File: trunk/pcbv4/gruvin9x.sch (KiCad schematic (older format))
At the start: 220 parts, among them IC1 ATMEGA2560-A_GRUVIN, J4 JUMPER_2W, K1 CONN_3, K2 CONN_3, K3 CONN_3, K4 CONN_3, P1 CONN_3X2, P10 CONN_5X2, P11 CONN_1, P12 CONN_4, P13 CONN_8, P14 CONN_2, P15 CONN_4, P16 CONN_1, P17 CONN_1, P18 CONN_2, P19 CONN_8, P2 CONN_5, P20 CONN_8, P21 CONN_4, P22 CONN_1, P23 CONN_1, P24 CONN_1, P25 CONN_1, P26 CONN_1, P27 CONN_2, P3 CONN_6, P4 CONN_9, P5 CONN_9, P6 CONN_6, P7 CONN_12, P8 CONN_30_LCD_GRUVIN, P9 CONN_1, Q1 BC847C, Q2 BC847C, Q3 BC857C, Q4 BC847C, Q5 BC847C, Q6 BC847C, Q7 BC847C, SW1 SW_PUSH, SW2 SW_PUSH, SW3 SW_PUSH, SW4 SW_PUSH, SW5 SW_PUSH, SW6 SW_PUSH, U1 78L05, U3 LN-6206-30, U4 TPS77601, X1 16MHz

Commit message: The keyboard 4x4 matrix has been removed to make the V4 board truly plug in compatible with the Tx. This has cost us 6 of our spare pins but well worth it in terms of palatability for a would be producer of the board. BOM updated. LED backlight finalized. Minor corrections of the footprint for the UK coin cell socket. More minor changes to...
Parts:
- removed D10, D11, D12, D13, D14, D15, D3, D4, D5, D6, D7, D8, D9: DIODESCH, symbol DIODESCH
- removed P19: CONN_8, symbol CONN_8
- removed P27: CONN_2, CONN_2MM_2x1, symbol CONN_2
- removed Q6: BC847C, SOT23-BCE, symbol BC847C
- added C37, C38, C39, C40, C41, C42, C43, C53, C54, C55, C56, C57, C58, C59, C60, C61: 0.1uF, symbol C
- added J1: JUMPER_2W, symbol JUMPER_2W
- added K5: CONN_3, symbol CONN_3
- added Q6: Si2319DS, symbol MOSFET_P
- added R100, R86, R87, R88, R89, R90, R97, R98, R99: 200R, symbol R
- added R101: 5K1, symbol R
- added U2: 78L05, SOT89, symbol 78L05
- R78: value 0R -> 200R
- R85: value 5K1 -> 100K
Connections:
- net labels added: Spare5, Spare6
- net labels removed: J1, J2, KEY_X0, KEY_X1, KEY_X2, KEY_X3, KEY_Y0, KEY_Y1, KEY_Y2, KEY_Y3
- wire segments 651 -> 685
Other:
- note removed: "(previously GNDs)"
- note removed: "4x4 Switch Matrix"
- note removed: "NOTE: Pull-ups for \nY0-Y3 MUST be off"
- note removed: "Navigation Buttons (reconfigured)"
- note removed: "Trim Switches"
- moved on the sheet: R85

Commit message: Missed off the 100R series resistor for the LED backlight. Put them on both of the switched rails, can be bridged out if not needed.
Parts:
- added R102, R103: 100R, symbol R
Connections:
- wire segments 685 -> 687
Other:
- moved on the sheet: K5
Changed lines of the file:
@@
-EESchema Schematic File Version 2  date 15/07/2011 16:46:34
+EESchema Schematic File Version 2  date 15/07/2011 18:05:00
 LIBS:device
 LIBS:transistors
@@
 $EndDescr
 Wire Wire Line
+	21300 11900 20000 11900
+Wire Wire Line
+	21800 12250 22200 12250
+Wire Wire Line
 	18600 13250 18600 13800
 Wire Wire Line
@@
 	18300 13250 18300 13450
 Wire Wire Line
-	21600 12450 21600 11900
-Wire Wire Line
-	21600 12450 21900 12450
-Wire Wire Line
-	21900 12350 21750 12350
+	22000 12450 22000 11900
+Wire Wire Line
+	22000 12450 22200 12450
+Wire Wire Line
+	22200 12350 22100 12350
 Wire Wire Line
 	19450 12600 19450 12550
@@
 Connection ~ 21200 12650
 Wire Wire Line
-	20000 12250 20000 11900
+	20000 11900 20000 12250
 Connection ~ 20600 12650
 Connection ~ 20000 12250
 Wire Wire Line
-	20200 12250 19650 12250
+	19650 12250 20200 12250
 Wire Wire Line
 	5950 12450 6400 12450
@@
 	10250 13900 10250 13650
 Wire Wire Line
-	10850 13650 9000 13650
+	9000 13650 10850 13650
 Connection ~ 10550 14400
 Wire Wire Line
@@
 	10450 13900 10450 13550
 Wire Wire Line
-	9000 13850 10850 13850
+	10850 13850 9000 13850
 Wire Wire Line
 	11450 13850 11350 13850
@@
 	10650 11850 9000 11850
 Wire Wire Line
-	7450 8750 7450 7750
+	7450 7750 7450 8750
 Wire Wire Line
 	7550 7900 7550 8750
@@
 	14450 9700 14450 9850
 Wire Wire Line
-	14400 9850 14900 9850
+	14900 9850 14400 9850
 Wire Wire Line
 	11350 3050 11850 3050
@@
 	10950 3750 10950 3850
 Wire Wire Line
-	11950 5100 10900 5100
+	10900 5100 11950 5100
 Wire Wire Line
 	17250 7750 17250 6100
@@
 	18650 9150 18650 10650
 Wire Wire Line
-	17300 8850 19100 8850
+	19100 8850 17300 8850
 Wire Wire Line
 	16250 7600 16250 7650
@@
 	9350 3450 9350 3600
 Wire Wire Line
-	6000 2650 4350 2650
+	4350 2650 6000 2650
 Wire Wire Line
 	15800 8500 15800 8450
@@
 	7000 2800 7000 2650
 Wire Wire Line
-	7000 3350 7000 3200
+	7000 3200 7000 3350
 Wire Wire Line
 	7350 3200 7350 3300
@@
 	6400 3200 6400 2950
 Wire Wire Line
-	5500 3200 5500 3300
+	5500 3300 5500 3200
 Connection ~ 4800 3300
 Wire Wire Line
@@
 Connection ~ 4800 2650
 Wire Wire Line
-	4800 2650 4800 2800
+	4800 2800 4800 2650
 Wire Wire Line
 	5100 10850 4450 10850
@@
 Connection ~ 5150 2650
 Wire Wire Line
-	4800 3350 4800 3200
+	4800 3200 4800 3350
 Wire Wire Line
 	5500 3900 5500 3800
@@
 	18000 6800 19050 6800
 Wire Wire Line
-	17150 7650 17600 7650
+	17600 7650 17150 7650
 Connection ~ 17550 7650
 Wire Wire Line
@@
 	19100 8650 17300 8650
 Wire Wire Line
-	16700 9400 16100 9400
-Wire Wire Line
-	15800 9200 15800 9000
+	16100 9400 16700 9400
+Wire Wire Line
+	15800 9000 15800 9200
 Connection ~ 15800 9100
 Wire Wire Line
 	7650 2650 7650 2600
 Wire Wire Line
-	5500 2700 5500 2650
+	5500 2650 5500 2700
 Connection ~ 5500 2650
 Wire Wire Line
@@
 	11500 5200 11500 5300
 Wire Wire Line
-	10500 3750 11100 3750
-Wire Wire Line
-	10650 3850 10650 3750
+	11100 3750 10500 3750
+Wire Wire Line
+	10650 3750 10650 3850
 Connection ~ 10650 3750
 Wire Wire Line
@@
 Connection ~ 10800 4400
 Wire Wire Line
-	10200 3350 10200 3550
+	10200 3550 10200 3350
 Wire Wire Line
 	11600 3750 11950 3750
@@
 	13100 7150 12150 7150
 Wire Wire Line
-	12150 7650 13100 7650
-Wire Wire Line
-	18450 7100 16750 7100
+	13100 7650 12150 7650
+Wire Wire Line
+	16750 7100 18450 7100
 Wire Wire Line
 	13100 7450 12150 7450
@@
 	9900 2750 9900 4700
 Wire Wire Line
-	10900 5000 11950 5000
+	11950 5000 10900 5000
 Wire Wire Line
 	11850 3050 11850 3100
@@
 	16350 13450 16350 13300
 Wire Wire Line
-	16650 12650 16450 12650
+	16450 12650 16650 12650
 Wire Wire Line
 	16550 12750 16550 12650
@@
 	13950 8950 14000 8950
 Wire Wire Line
-	12150 7750 13100 7750
+	13100 7750 12150 7750
 Wire Wire Line
 	10650 9950 9000 9950
@@
 	13850 9650 13800 9650
 Wire Wire Line
-	7850 8500 7850 8750
+	7850 8750 7850 8500
 Wire Wire Line
 	8500 8550 8400 8550
@@
 	6700 5900 6700 6000
 Wire Wire Line
-	7750 14550 7450 14550
+	7450 14550 7750 14550
 Wire Wire Line
 	6400 13750 6050 13750
@@
 	14500 15150 14500 15250
 Wire Wire Line
-	16050 15600 16050 14850
+	16050 14850 16050 15600
 Wire Wire Line
 	15800 14850 15800 14950
@@
 	11450 13550 11000 13550
 Wire Wire Line
-	10500 13550 9000 13550
+	9000 13550 10500 13550
 Wire Wire Line
 	10650 13900 10650 13850
@@
 Connection ~ 10450 14400
 Wire Wire Line
-	9000 13750 10500 13750
-Wire Wire Line
-	10650 14400 10050 14400
+	10500 13750 9000 13750
+Wire Wire Line
+	10050 14400 10650 14400
 Connection ~ 10250 14400
 Wire Wire Line
@@
 Connection ~ 16600 9750
 Wire Wire Line
-	15800 9600 15800 10150
+	15800 10150 15800 9600
 Connection ~ 15800 10000
 Wire Wire Line
@@
 Connection ~ 21200 12250
 Wire Wire Line
-	20600 12550 20600 12800
+	20600 12800 20600 12550
 Wire Wire Line
 	18750 12250 18750 12550
@@
 	18300 13450 19000 13450
 Wire Wire Line
-	21000 12250 21900 12250
-Wire Wire Line
-	20000 11900 21600 11900
-Wire Wire Line
-	21750 12350 21750 12650
-Wire Wire Line
-	21750 12650 20000 12650
-Wire Wire Line
-	18300 12250 19250 12250
+	22100 12350 22100 12650
+Wire Wire Line
+	22100 12650 20000 12650
+Wire Wire Line
+	19250 12250 18300 12250
 Connection ~ 18750 12250
 Wire Wire Line
@@
 Wire Wire Line
 	18000 13550 18000 13250
+Wire Wire Line
+	21300 12250 21000 12250
+Wire Wire Line
+	22000 11900 21800 11900
+$Comp
+L R R103
+U 1 1 4E207322
+P 21550 11900
+F 0 "R103" V 21630 11900 50  0000 C CNN
+F 1 "100R" V 21550 11900 50  0000 C CNN
+	1    21550 11900
+	0    -1   -1   0
+$EndComp
+$Comp
+L R R102
+U 1 1 4E2072D1
+P 21550 12250
+F 0 "R102" V 21630 12250 50  0000 C CNN
+F 1 "100R" V 21550 12250 50  0000 C CNN
+	1    21550 12250
+	0    -1   -1   0
+$EndComp
 Text Label 17650 13550 0    60   ~ 0
 Spare3
@@
 L CONN_3 K5
 U 1 1 4E20326D
-P 22250 12350
-F 0 "K5" V 22200 12350 50  0000 C CNN
-F 1 "CONN_3" V 22300 12350 40  0000 C CNN
-	1    22250 12350
+P 22550 12350
+F 0 "K5" V 22500 12350 50  0000 C CNN
+F 1 "CONN_3" V 22600 12350 40  0000 C CNN
+	1    22550 12350
 	1    0    0    -1
 $EndComp

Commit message: Some pin swaps on the V4 PCB
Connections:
- net labels added: DOWN_P, EXIT_P, LEFT_P, LH_Dwn_P, LH_Up_P, LV_Dwn_P, LV_Up_P, MENU_P, RH_Dwn_P, RH_Up_P, RIGHT_P, RV_Dwn_P, RV_Up_P, UP_P
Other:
- moved on the sheet: P11, P16, P17, P22, P23, P24, P9, R100, R13, R14, R21, R22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

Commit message: One more feature addition, as per ronson's request. And a few pin changes to make the rotary encoders neater to code.
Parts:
- removed P11, P22: CONN_1, symbol CONN_1
- added D3, D4: 3.6v, symbol ZENER
- added K6: CONN_3, symbol CONN_3
- added R104, R105: 68R, symbol R
- added R106, R107, R108, R109, R110: 1.5K, symbol R
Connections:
- net labels added: USB_D+, USB_D-
- net labels removed: Spare1, Spare2
- wire segments 687 -> 682
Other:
- moved on the sheet: C1, C10, C12, C15, C2, C22, C23, C24, C25, C26, C27, C28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

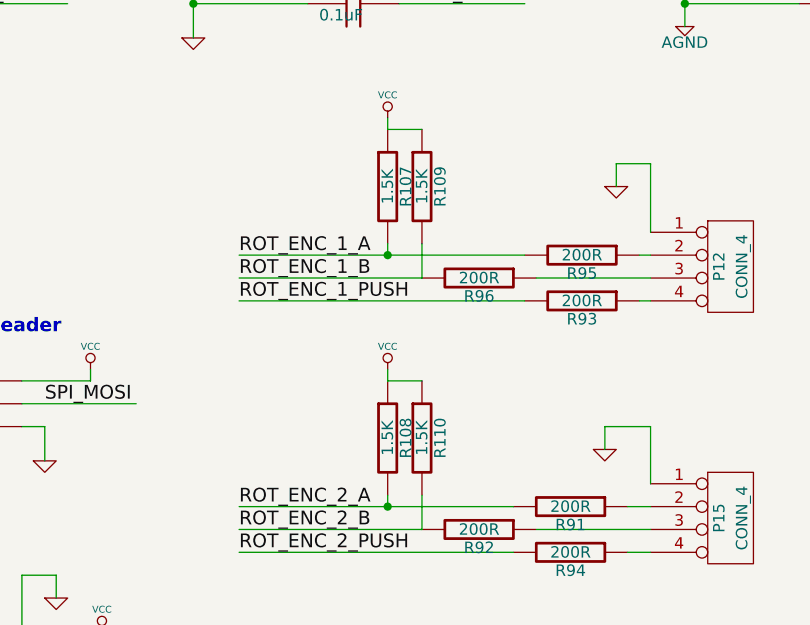
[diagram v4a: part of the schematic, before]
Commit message: V4 BOM update, diode footprints now look like diodes, trace thickening in places
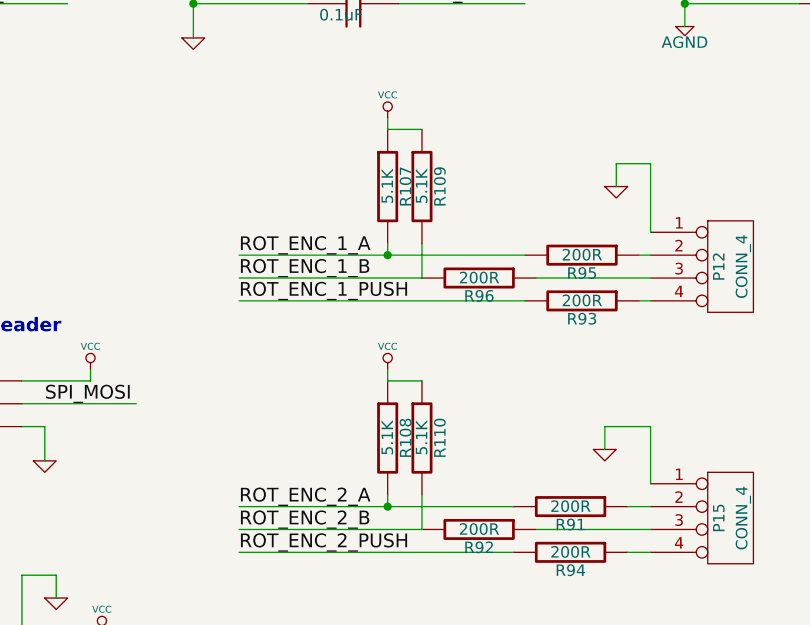
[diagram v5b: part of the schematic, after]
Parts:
- R107, R108, R109, R110: value 1.5K -> 5.1K
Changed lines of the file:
@@
-EESchema Schematic File Version 2  date 23/07/2011 17:05:19
+EESchema Schematic File Version 2  date 24/07/2011 22:09:50
 LIBS:device
 LIBS:transistors
@@
 Sheet 1 1
 Title "Main Controller PCB for 100pin ATMega"
-Date "23 jul 2011"
+Date "24 jul 2011"
 Rev "4.0"
 Comp ""
@@
 P 5850 6800
 F 0 "R110" V 5930 6800 50  0000 C CNN
-F 1 "1.5K" V 5850 6800 50  0000 C CNN
+F 1 "5.1K" V 5850 6800 50  0000 C CNN
 	1    5850 6800
 	1    0    0    -1
@@
 P 5700 6800
 F 0 "R108" V 5780 6800 50  0000 C CNN
-F 1 "1.5K" V 5700 6800 50  0000 C CNN
+F 1 "5.1K" V 5700 6800 50  0000 C CNN
 	1    5700 6800
 	1    0    0    -1
@@
 P 5850 5700
 F 0 "R109" V 5930 5700 50  0000 C CNN
-F 1 "1.5K" V 5850 5700 50  0000 C CNN
+F 1 "5.1K" V 5850 5700 50  0000 C CNN
 	1    5850 5700
 	1    0    0    -1
@@
 P 5700 5700
 F 0 "R107" V 5780 5700 50  0000 C CNN
-F 1 "1.5K" V 5700 5700 50  0000 C CNN
+F 1 "5.1K" V 5700 5700 50  0000 C CNN
 	1    5700 5700
 	1    0    0    -1

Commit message: Update of final V4 PCB changes
Inclusion of 1.2v reference for the ADC.
These boards are now at the factory.
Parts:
- removed P21: CONN_4, symbol CONN_4
- removed R32: 10K2, symbol R
- added C62: 1uF, symbol C
- added P21: CONN_3, symbol CONN_3
- added U5: REF3012, SOT89, symbol 78L05
- R24: value 5K1 -> 200R
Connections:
- net labels added: +1.2V
- wire segments 682 -> 691
